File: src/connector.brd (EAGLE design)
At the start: 54 x 8.1 mm, 2 parts

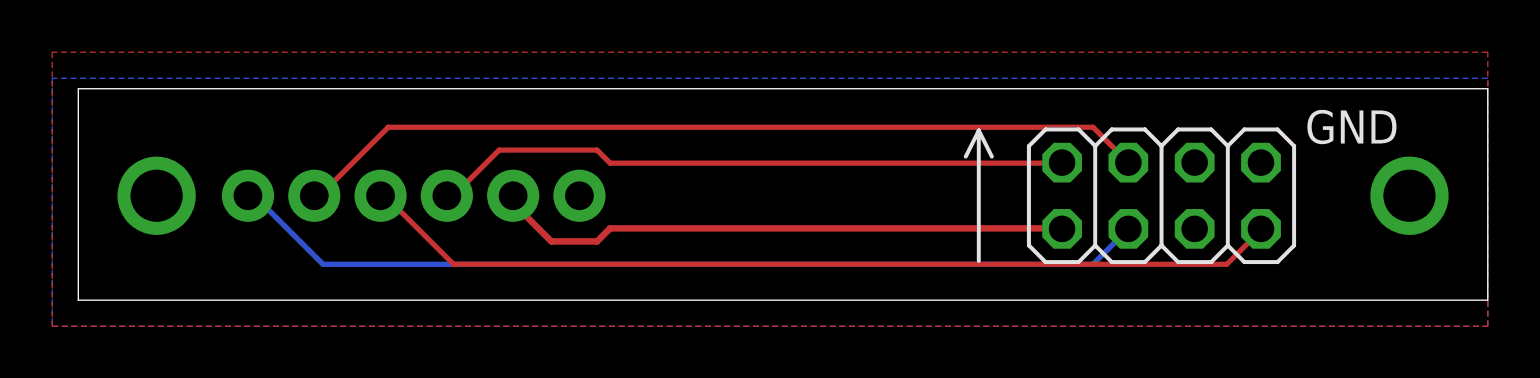
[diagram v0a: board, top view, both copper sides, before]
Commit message: Improved layout of connector board
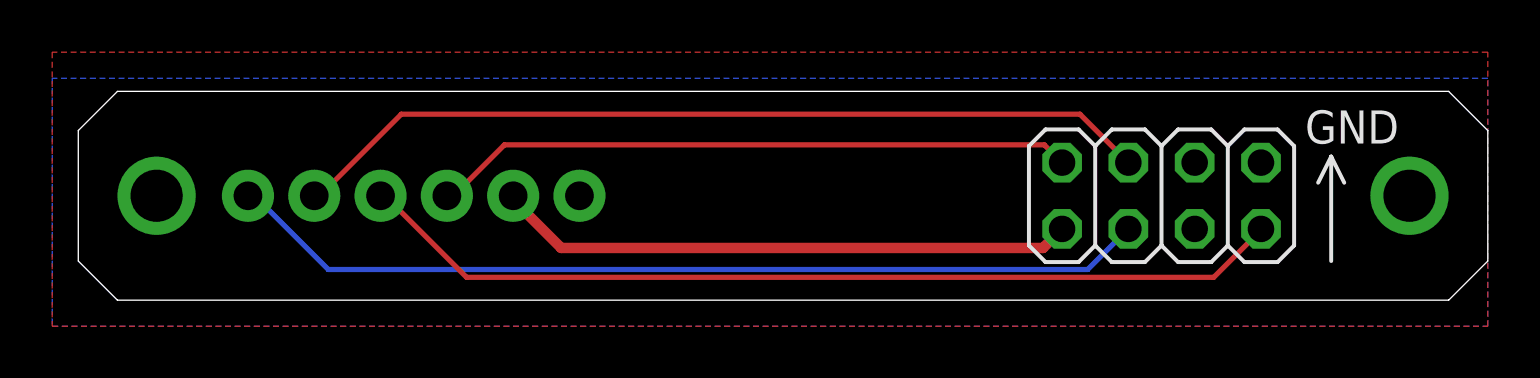
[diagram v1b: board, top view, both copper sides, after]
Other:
- board size 54 x 8.1 mm -> 54 x 8 mm
- board text added: "URU Card"
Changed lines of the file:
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@@
 <drawing>
 <settings>
-<setting alwaysvectorfont="no"/>
+<setting alwaysvectorfont="yes"/>
 <setting verticaltext="up"/>
 </settings>
-<grid distance="0.5" unitdist="mm" unit="mm" style="lines" multiple="1" display="yes" altdistance="0.05" altunitdist="mm" altunit="mm"/>
+<grid distance="0.1" unitdist="mm" unit="mm" style="lines" multiple="1" display="yes" altdistance="0.05" altunitdist="mm" altunit="mm"/>
 <layers>
 <layer number="1" name="Top" color="4" fill="1" visible="yes" active="yes"/>
@@
 <board>
 <plain>
-<wire x1="0" y1="0" x2="54" y2="0" width="0" layer="20"/>
-<wire x1="54" y1="0" x2="54" y2="8.1" width="0" layer="20"/>
-<wire x1="54" y1="8.1" x2="0" y2="8.1" width="0" layer="20"/>
-<wire x1="0" y1="8.1" x2="0" y2="0" width="0" layer="20"/>
+<wire x1="0" y1="1.5" x2="1.5" y2="0" width="0" layer="20"/>
+<wire x1="1.5" y1="0" x2="52.5" y2="0" width="0" layer="20"/>
+<wire x1="52.5" y1="0" x2="54" y2="1.5" width="0" layer="20"/>
+<wire x1="54" y1="1.5" x2="54" y2="6.5" width="0" layer="20"/>
+<wire x1="54" y1="6.5" x2="52.5" y2="8" width="0" layer="20"/>
+<wire x1="52.5" y1="8" x2="1.5" y2="8" width="0" layer="20"/>
+<wire x1="1.5" y1="8" x2="0" y2="6.5" width="0" layer="20"/>
 <text x="50" y="6" size="1.27" layer="22" font="vector" rot="MR0">GND</text>
 <text x="47" y="6" size="1.27" layer="21" font="vector">GND</text>
-<wire x1="34.5" y1="6.5" x2="34.5" y2="1.5" width="0.1524" layer="21"/>
-<wire x1="35" y1="5.5" x2="34.5" y2="6.5" width="0.1524" layer="21"/>
-<wire x1="34.5" y1="6.5" x2="34" y2="5.5" width="0.1524" layer="21"/>
-<wire x1="34.5" y1="1.5" x2="34.5" y2="6.5" width="0.1524" layer="22"/>
-<wire x1="35" y1="5.5" x2="34.5" y2="6.5" width="0.1524" layer="22"/>
-<wire x1="34" y1="5.5" x2="34.5" y2="6.5" width="0.1524" layer="22"/>
+<wire x1="0" y1="6.5" x2="0" y2="1.5" width="0" layer="20"/>
+<wire x1="48" y1="5.5" x2="48" y2="1.5" width="0.1524" layer="21"/>
+<wire x1="48.5" y1="4.5" x2="48" y2="5.5" width="0.1524" layer="21"/>
+<wire x1="48" y1="5.5" x2="47.5" y2="4.5" width="0.1524" layer="21"/>
+<wire x1="48" y1="1.5" x2="48" y2="5.5" width="0.1524" layer="22"/>
+<wire x1="48.5" y1="4.5" x2="48" y2="5.5" width="0.1524" layer="22"/>
+<wire x1="47.5" y1="4.5" x2="48" y2="5.5" width="0.1524" layer="22"/>
+<text x="35.5" y="3" size="2.54" layer="22" font="vector" ratio="15" rot="MR0">URU Card</text>
 </plain>
 <attributes>
@@
 <signals>
 <signal name="GND" class="2">
-<polygon width="0.1524" layer="1">
+<polygon width="0.4" layer="1">
 <vertex x="-1" y="-1"/>
 <vertex x="54" y="-1"/>
@@
 <vertex x="-1" y="9.5"/>
 </polygon>
-<polygon width="0.1524" layer="16">
+<polygon width="0.4" layer="16">
 <vertex x="-1" y="-1"/>
 <vertex x="54" y="-1"/>
@@
 <contactref element="U$16" pad="P$5"/>
 <contactref element="JP1" pad="8"/>
-<wire x1="20.375" y1="2.75" x2="37.625" y2="2.75" width="0.25" layer="1"/>
-<wire x1="19.875" y1="2.25" x2="20.375" y2="2.75" width="0.25" layer="1"/>
-<wire x1="18.125" y1="2.25" x2="19.875" y2="2.25" width="0.25" layer="1"/>
-<wire x1="16.75" y1="3.625" x2="18.125" y2="2.25" width="0.25" layer="1"/>
-<wire x1="16.75" y1="4" x2="16.75" y2="3.625" width="0.25" layer="1"/>
-<wire x1="37.625" y1="2.75" x2="37.69" y2="2.73" width="0.25" layer="1"/>
-<wire x1="16.75" y1="4" x2="16.66" y2="4" width="0.25" layer="1"/>
+<wire x1="37.69" y1="2.73" x2="36.96" y2="2" width="0.4" layer="1"/>
+<wire x1="36.96" y1="2" x2="18.5" y2="2" width="0.4" layer="1"/>
+<wire x1="18.5" y1="2" x2="16.66" y2="3.84" width="0.4" layer="1"/>
+<wire x1="16.66" y1="3.84" x2="16.66" y2="4" width="0.4" layer="1"/>
 </signal>
 <signal name="TXD">
 <contactref element="U$16" pad="P$4"/>
 <contactref element="JP1" pad="7"/>
-<wire x1="20.375" y1="5.25" x2="37.625" y2="5.25" width="0.2" layer="1"/>
-<wire x1="19.875" y1="5.75" x2="20.375" y2="5.25" width="0.2" layer="1"/>
-<wire x1="16.125" y1="5.75" x2="19.875" y2="5.75" width="0.2" layer="1"/>
-<wire x1="14.375" y1="4" x2="16.125" y2="5.75" width="0.2" layer="1"/>
+<wire x1="37.69" y1="5.27" x2="37.01" y2="5.95" width="0.2" layer="1"/>
+<wire x1="37.01" y1="5.95" x2="16.325" y2="5.95" width="0.2" layer="1"/>
+<wire x1="14.375" y1="4" x2="16.325" y2="5.95" width="0.2" layer="1"/>
 <wire x1="14.12" y1="4" x2="14.375" y2="4" width="0.2" layer="1"/>
-<wire x1="37.625" y1="5.25" x2="37.69" y2="5.27" width="0.2" layer="1"/>
 </signal>
 <signal name="RXD">
 <contactref element="U$16" pad="P$3"/>
 <contactref element="JP1" pad="2"/>
-<wire x1="44" y1="1.375" x2="45.25" y2="2.625" width="0.2" layer="1"/>
-<wire x1="14.375" y1="1.375" x2="44" y2="1.375" width="0.2" layer="1"/>
-<wire x1="11.75" y1="4" x2="14.375" y2="1.375" width="0.2" layer="1"/>
+<wire x1="43.5" y1="0.875" x2="45.25" y2="2.625" width="0.2" layer="1"/>
+<wire x1="14.875" y1="0.875" x2="43.5" y2="0.875" width="0.2" layer="1"/>
+<wire x1="11.75" y1="4" x2="14.875" y2="0.875" width="0.2" layer="1"/>
 <wire x1="11.58" y1="4" x2="11.75" y2="4" width="0.2" layer="1"/>
 <wire x1="45.25" y1="2.625" x2="45.31" y2="2.73" width="0.2" layer="1"/>
@@
 <contactref element="U$16" pad="P$1"/>
 <contactref element="JP1" pad="6"/>
-<wire x1="38.875" y1="1.375" x2="40.23" y2="2.73" width="0.2" layer="16"/>
-<wire x1="9.375" y1="1.375" x2="38.875" y2="1.375" width="0.2" layer="16"/>
-<wire x1="6.75" y1="4" x2="9.375" y2="1.375" width="0.2" layer="16"/>
+<wire x1="38.675" y1="1.175" x2="40.23" y2="2.73" width="0.2" layer="16"/>
+<wire x1="9.575" y1="1.175" x2="38.675" y2="1.175" width="0.2" layer="16"/>
+<wire x1="6.75" y1="4" x2="9.575" y2="1.175" width="0.2" layer="16"/>
 <wire x1="6.5" y1="4" x2="6.75" y2="4" width="0.2" layer="16"/>
 </signal>
@@
 <contactref element="U$16" pad="P$2"/>
 <contactref element="JP1" pad="5"/>
-<wire x1="38.875" y1="6.625" x2="40.23" y2="5.27" width="0.2" layer="1"/>
-<wire x1="11.875" y1="6.625" x2="38.875" y2="6.625" width="0.2" layer="1"/>
-<wire x1="9.25" y1="4" x2="11.875" y2="6.625" width="0.2" layer="1"/>
+<wire x1="38.375" y1="7.125" x2="40.23" y2="5.27" width="0.2" layer="1"/>
+<wire x1="12.375" y1="7.125" x2="38.375" y2="7.125" width="0.2" layer="1"/>
+<wire x1="9.25" y1="4" x2="12.375" y2="7.125" width="0.2" layer="1"/>
 <wire x1="9.04" y1="4" x2="9.25" y2="4" width="0.2" layer="1"/>
 </signal>
